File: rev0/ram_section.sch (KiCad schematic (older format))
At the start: 5 parts

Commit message: rev0: finish capture and start routing (woo!)
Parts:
- C44, C45, C46: renamed from C?; footprint (none) -> Capacitor_SMD:C_0402_1005Metric
- IC1: renamed from IC?; footprint BGA256C80P16X16_1400X1400X170 -> luna:lattice_cabga256
- gave numbers to parts that had none: 1
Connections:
- no-connect marks 5 -> 24
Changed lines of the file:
@@
 	1850 1800 1900 1800
 $Comp
-L power:+1V8 #PWR?
+L power:+1V8 #PWR081
 U 1 1 5DE84804
 P 1850 1700
-F 0 "#PWR?" H 1850 1550 50  0001 C CNN
+F 0 "#PWR081" H 1850 1550 50  0001 C CNN
 F 1 "+1V8" H 1864 1873 50  0000 C CNN
 F 2 "" H 1850 1700 50  0001 C CNN
@@
 $EndComp
 $Comp
-L fpgas_and_processors:ECP5-BGA256 IC?
+L fpgas_and_processors:ECP5-BGA256 IC1
 U 3 1 5DE93650
 P 1650 2100
-F 0 "IC?" H 1620 308 50  0000 R CNN
+F 0 "IC1" H 1620 308 50  0000 R CNN
 F 1 "ECP5-BGA256" H 1620 218 50  0000 R CNN
-F 2 "BGA256C80P16X16_1400X1400X170" H -1550 5550 50  0001 L CNN
+F 2 "luna:lattice_cabga256" H -1550 5550 50  0001 L CNN
 F 3 "" H -2000 6500 50  0001 L CNN
 F 4 "FPGA - Field Programmable Gate Array ECP5; 12k LUTs; 1.1V" H -2000 6400 50  0001 L CNN "Description"
@@
 $EndComp
 $Comp
-L support_hardware:S27KS0641 U?
+L support_hardware:S27KS0641 U10
 U 1 1 5DEA1FC4
 P 5400 4850
-F 0 "U?" H 5400 5772 50  0000 C CNN
+F 0 "U10" H 5400 5772 50  0000 C CNN
 F 1 "S27KS0641" H 5400 5682 50  0000 C CNN
 F 2 "pkl_housings_bga:BGA-24_5x5_6.0x8.0mm" H 6000 3950 50  0001 C CNN
@@
 	6550 4250 6550 4000
 $Comp
-L power:+1V8 #PWR?
+L power:+1V8 #PWR084
 U 1 1 5DEA6771
 P 6550 4000
-F 0 "#PWR?" H 6550 3850 50  0001 C CNN
+F 0 "#PWR084" H 6550 3850 50  0001 C CNN
 F 1 "+1V8" H 6564 4173 50  0000 C CNN
 F 2 "" H 6550 4000 50  0001 C CNN
@@
 	6550 5450 6550 5600
 $Comp
-L power:GND #PWR?
+L power:GND #PWR085
 U 1 1 5DEA82D8
 P 6550 5600
-F 0 "#PWR?" H 6550 5350 50  0001 C CNN
+F 0 "#PWR085" H 6550 5350 50  0001 C CNN
 F 1 "GND" H 6554 5428 50  0000 C CNN
 F 2 "" H 6550 5600 50  0001 C CNN
@@
 	6350 4550 6000 4550
 $Comp
-L Device:C C?
+L Device:C C44
 U 1 1 5DEC975A
 P 5100 3050
-F 0 "C?" H 5150 3150 50  0000 L CNN
+F 0 "C44" H 5150 3150 50  0000 L CNN
 F 1 "0.1uF" H 5150 2950 50  0000 L CNN
-F 2 "" H 5138 2900 50  0001 C CNN
+F 2 "Capacitor_SMD:C_0402_1005Metric" H 5138 2900 50  0001 C CNN
 F 3 "~" H 5100 3050 50  0001 C CNN
 	1    5100 3050
@@
 $EndComp
 $Comp
-L Device:C C?
+L Device:C C45
 U 1 1 5DECBE47
 P 5400 3050
-F 0 "C?" H 5450 3150 50  0000 L CNN
+F 0 "C45" H 5450 3150 50  0000 L CNN
 F 1 "0.1uF" H 5450 2950 50  0000 L CNN
-F 2 "" H 5438 2900 50  0001 C CNN
+F 2 "Capacitor_SMD:C_0402_1005Metric" H 5438 2900 50  0001 C CNN
 F 3 "~" H 5400 3050 50  0001 C CNN
 	1    5400 3050
@@
 $EndComp
 $Comp
-L Device:C C?
+L Device:C C46
 U 1 1 5DECC0D1
 P 5700 3050
-F 0 "C?" H 5750 3150 50  0000 L CNN
+F 0 "C46" H 5750 3150 50  0000 L CNN
 F 1 "0.1uF" H 5750 2950 50  0000 L CNN
-F 2 "" H 5738 2900 50  0001 C CNN
+F 2 "Capacitor_SMD:C_0402_1005Metric" H 5738 2900 50  0001 C CNN
 F 3 "~" H 5700 3050 50  0001 C CNN
 	1    5700 3050
@@
 	5400 2800 5700 2800
 $Comp
-L power:+5V #PWR?
+L power:+5V #PWR082
 U 1 1 5DECF10E
 P 5400 2650
-F 0 "#PWR?" H 5400 2500 50  0001 C CNN
+F 0 "#PWR082" H 5400 2500 50  0001 C CNN
 F 1 "+5V" H 5414 2823 50  0000 C CNN
 F 2 "" H 5400 2650 50  0001 C CNN
@@
 Wire Wire Line
 	5400 3300 5400 3400
-Wire Bus Line
-	3100 5650 3100 6050
-Wire Bus Line
-	7200 4950 7200 6050
-$Comp
-L power:GND #PWR?
+$Comp
+L power:GND #PWR083
 U 1 1 5DED5068
 P 5400 3400
-F 0 "#PWR?" H 5400 3150 50  0001 C CNN
+F 0 "#PWR083" H 5400 3150 50  0001 C CNN
 F 1 "GND" H 5404 3228 50  0000 C CNN
 F 2 "" H 5400 3400 50  0001 C CNN
@@
 Text Label 4000 5150 0    50   ~ 0
 RAM_RWDS
+NoConn ~ 2700 2550
+NoConn ~ 2700 2650
+NoConn ~ 2700 2750
+NoConn ~ 2700 2850
+NoConn ~ 2700 2950
+NoConn ~ 2700 3050
+NoConn ~ 2700 3150
+NoConn ~ 2700 3250
+NoConn ~ 2700 3650
+NoConn ~ 2700 3750
+NoConn ~ 2700 3850
+NoConn ~ 2700 4050
+NoConn ~ 2700 4150
+NoConn ~ 2700 4650
+NoConn ~ 2700 4750
+NoConn ~ 2700 4850
+NoConn ~ 2700 5050
+NoConn ~ 2700 5150
+NoConn ~ 2700 5250
+Wire Bus Line
+	3100 5650 3100 6050
+Wire Bus Line
+	7200 4950 7200 6050
 $EndSCHEMATC

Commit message: rev0: throw the parts down so we can get starting routing
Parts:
- U10: footprint pkl_housings_bga:BGA-24_5x5_6.0x8.0mm -> luna:BGA-24_5x5_6.0x8.0mm
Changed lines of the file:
@@
 F 0 "U10" H 5400 5772 50  0000 C CNN
 F 1 "S27KS0641" H 5400 5682 50  0000 C CNN
-F 2 "pkl_housings_bga:BGA-24_5x5_6.0x8.0mm" H 6000 3950 50  0001 C CNN
+F 2 "luna:BGA-24_5x5_6.0x8.0mm" H 6000 3950 50  0001 C CNN
 F 3 "" H 5400 3950 50  0001 C CNN
 F 4 "ANY" H 5400 4850 50  0001 C CNN "Source"

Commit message: rev0: more routing scaffolding
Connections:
- net RAM_DQ3: now also IC1.B9 (PT38A); no longer IC1.E11 (PT51B)
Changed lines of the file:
@@
 	3500 4650 4800 4650
-Wire Wire Line
-	2700 4250 3400 4250
-Wire Wire Line
-	3400 4250 3400 4750
 Wire Wire Line
 	3400 4750 4800 4750
@@
 NoConn ~ 2700 2750
 NoConn ~ 2700 2850
-NoConn ~ 2700 2950
 NoConn ~ 2700 3050
 NoConn ~ 2700 3150
@@
 NoConn ~ 2700 5150
 NoConn ~ 2700 5250
+Wire Wire Line
+	2700 2950 3400 2950
+Wire Wire Line
+	3400 2950 3400 4750
+NoConn ~ 2700 4250
 Wire Bus Line
 	3100 5650 3100 6050

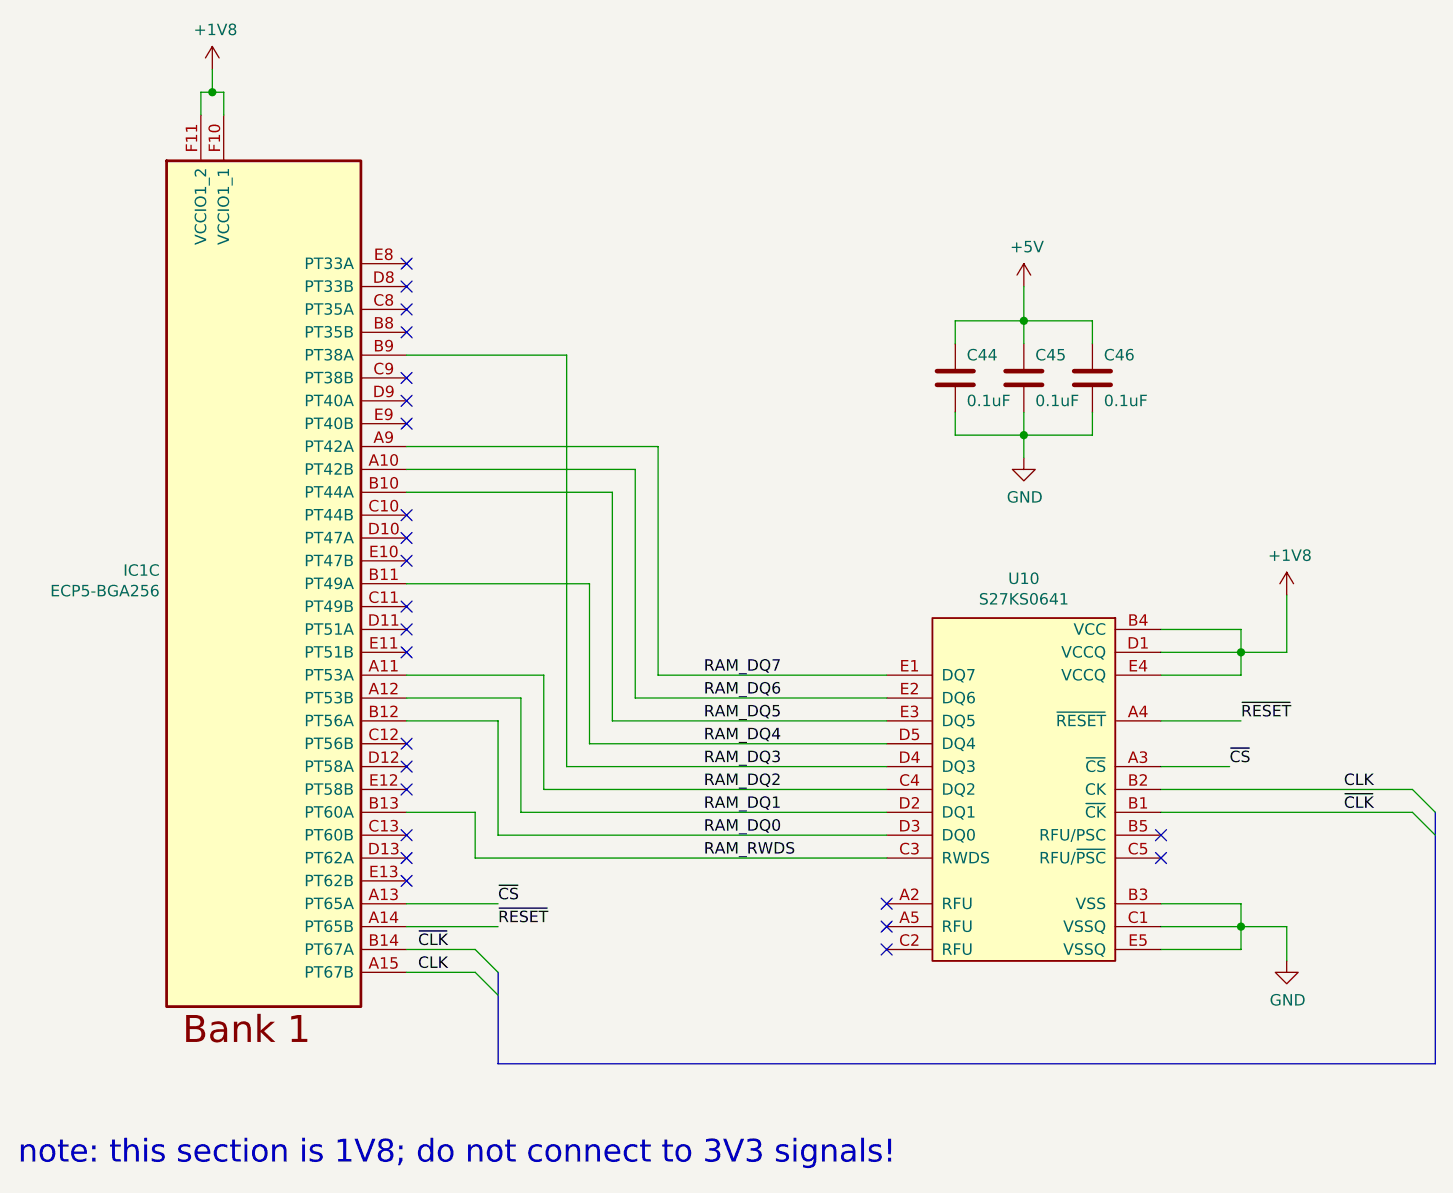
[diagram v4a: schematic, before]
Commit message: rev0: get most of the major routing done
still needs power routing, length matching for the busses,
and routing for the misc control stuff
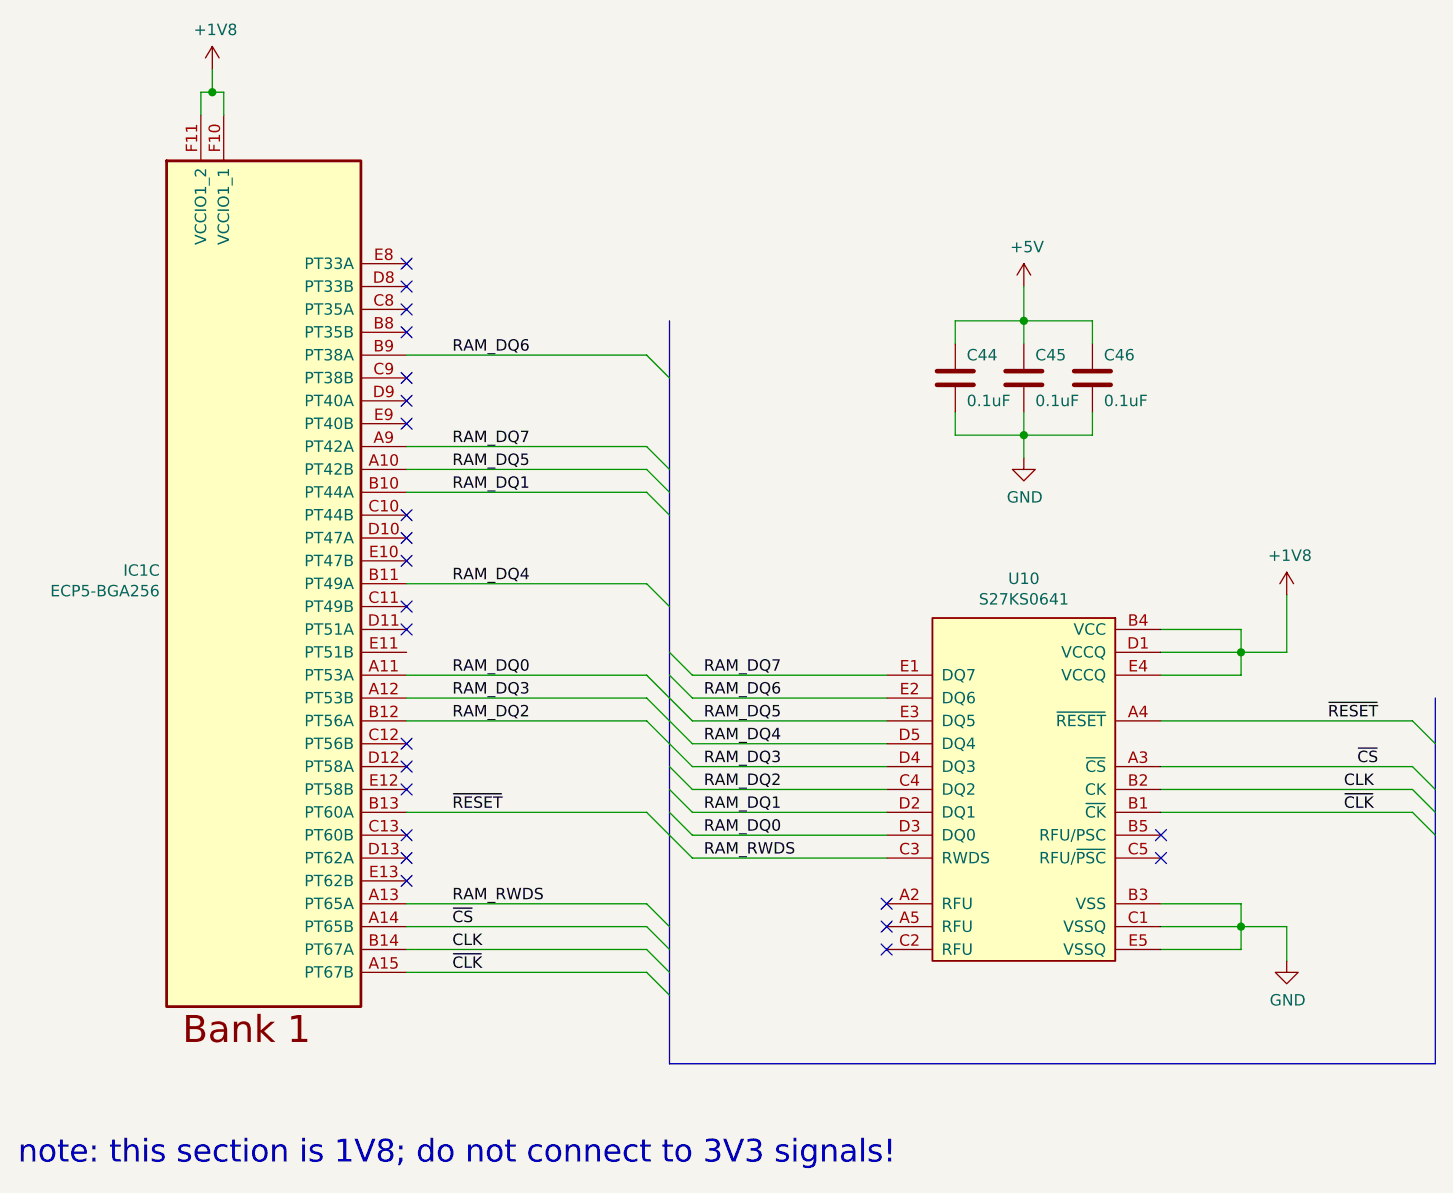
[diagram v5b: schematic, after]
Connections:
- net CLK: now also IC1.B14 (PT67A); no longer IC1.A15 (PT67B)
- net RAM_DQ0: now also IC1.A11 (PT53A); no longer IC1.B12 (PT56A)
- net RAM_DQ1: now also IC1.B10 (PT44A); no longer IC1.A12 (PT53B)
- net RAM_DQ2: now also IC1.B12 (PT56A); no longer IC1.A11 (PT53A)
- net RAM_DQ3: now also IC1.A12 (PT53B); no longer IC1.B9 (PT38A)
- net RAM_DQ5: now also IC1.A10 (PT42B); no longer IC1.B10 (PT44A)
- net RAM_DQ6: now also IC1.B9 (PT38A); no longer IC1.A10 (PT42B)
- net RAM_RWDS: now also IC1.A13 (PT65A); no longer IC1.B13 (PT60A)
- net ~CLK: now also IC1.A15 (PT67B); no longer IC1.B14 (PT67A)
- net ~CS: now also IC1.A14 (PT65B); no longer IC1.A13 (PT65A)
- net ~RESET: now also IC1.B13 (PT60A); no longer IC1.A14 (PT65B)
- no-connect marks 24 -> 23
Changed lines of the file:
@@
 Entry Wire Line
 	7100 4950 7200 5050
-Wire Wire Line
-	2700 5550 3000 5550
-Wire Wire Line
-	2700 5650 3000 5650
-Entry Wire Line
-	3000 5550 3100 5650
-Entry Wire Line
-	3000 5650 3100 5750
 Text Label 6800 4850 0    50   ~ 0
 CLK
 Text Label 6800 4950 0    50   ~ 0
 ~CLK
-Wire Bus Line
-	3100 6050 7200 6050
-Text Label 2750 5550 0    50   ~ 0
+Text Label 2900 5650 0    50   ~ 0
 ~CLK
-Text Label 2750 5650 0    50   ~ 0
+Text Label 2900 5550 0    50   ~ 0
 CLK
-Wire Wire Line
-	2700 3350 3800 3350
-Wire Wire Line
-	3800 3350 3800 4350
-Wire Wire Line
-	3800 4350 4800 4350
-Wire Wire Line
-	2700 3450 3700 3450
-Wire Wire Line
-	3700 3450 3700 4450
-Wire Wire Line
-	3700 4450 4800 4450
-Wire Wire Line
-	2700 3550 3600 3550
-Wire Wire Line
-	3600 3550 3600 4550
-Wire Wire Line
-	3600 4550 4800 4550
-Wire Wire Line
-	2700 3950 3500 3950
-Wire Wire Line
-	3500 3950 3500 4650
-Wire Wire Line
-	3500 4650 4800 4650
-Wire Wire Line
-	3400 4750 4800 4750
-Wire Wire Line
-	2700 4350 3300 4350
-Wire Wire Line
-	3300 4350 3300 4850
-Wire Wire Line
-	3300 4850 4800 4850
-Wire Wire Line
-	2700 4450 3200 4450
-Wire Wire Line
-	3200 4450 3200 4950
-Wire Wire Line
-	3200 4950 4800 4950
-Wire Wire Line
-	2700 4550 3100 4550
-Wire Wire Line
-	3100 4550 3100 5050
-Wire Wire Line
-	3100 5050 4800 5050
-Wire Wire Line
-	4800 5150 3000 5150
-Wire Wire Line
-	3000 5150 3000 4950
-Wire Wire Line
-	3000 4950 2700 4950
 NoConn ~ 4800 5350
 NoConn ~ 4800 5450
@@
 NoConn ~ 6000 5050
 NoConn ~ 6000 5150
-Wire Wire Line
-	2700 5450 3100 5450
-Text Label 3100 5350 0    50   ~ 0
+Text Label 2900 5450 0    50   ~ 0
 ~CS
-Wire Wire Line
-	6000 4750 6300 4750
-Text Label 6300 4750 0    50   ~ 0
+Text Label 6950 4750 2    50   ~ 0
 ~CS
-Wire Wire Line
-	2700 5350 3100 5350
-Text Label 3100 5450 0    50   ~ 0
+Text Label 2900 4950 0    50   ~ 0
 ~RESET
-Text Label 6350 4550 0    50   ~ 0
+Text Label 6950 4550 2    50   ~ 0
 ~RESET
-Wire Wire Line
-	6350 4550 6000 4550
 $Comp
 L Device:C C44
@@
 NoConn ~ 2700 5250
 Wire Wire Line
-	2700 2950 3400 2950
-Wire Wire Line
-	3400 2950 3400 4750
-NoConn ~ 2700 4250
+	4800 4350 3950 4350
+Wire Wire Line
+	3950 4450 4800 4450
+Wire Wire Line
+	4800 4550 3950 4550
+Wire Wire Line
+	4800 4650 3950 4650
+Wire Wire Line
+	4800 4750 3950 4750
+Wire Wire Line
+	4800 4850 3950 4850
+Wire Wire Line
+	4800 4950 3950 4950
+Wire Wire Line
+	4800 5050 3950 5050
+Wire Wire Line
+	4800 5150 3950 5150
+Entry Wire Line
+	3850 4250 3950 4350
+Entry Wire Line
+	3850 4350 3950 4450
+Entry Wire Line
+	3850 4450 3950 4550
+Entry Wire Line
+	3850 4550 3950 4650
+Entry Wire Line
+	3850 4650 3950 4750
+Entry Wire Line
+	3850 4750 3950 4850
+Entry Wire Line
+	3850 4850 3950 4950
+Entry Wire Line
+	3850 4950 3950 5050
+Entry Wire Line
+	3850 5050 3950 5150
 Wire Bus Line
-	3100 5650 3100 6050
+	3850 6050 7200 6050
+Wire Wire Line
+	2700 3350 3750 3350
+Wire Wire Line
+	2700 3450 3750 3450
+Wire Wire Line
+	2700 2950 3750 2950
+Wire Wire Line
+	2700 3550 3750 3550
+Entry Wire Line
+	3750 2950 3850 3050
+Entry Wire Line
+	3750 3350 3850 3450
+Entry Wire Line
+	3750 3450 3850 3550
+Entry Wire Line
+	3750 3550 3850 3650
+Text Label 2900 3350 0    50   ~ 0
+RAM_DQ7
+Text Label 2900 2950 0    50   ~ 0
+RAM_DQ6
+Text Label 2900 3450 0    50   ~ 0
+RAM_DQ5
+Text Label 2900 3550 0    50   ~ 0
+RAM_DQ1
+Wire Wire Line
+	2700 3950 3750 3950
+Entry Wire Line
+	3750 3950 3850 4050
+Text Label 2900 4350 0    50   ~ 0
+RAM_DQ0
+Text Label 2900 3950 0    50   ~ 0
+RAM_DQ4
+Wire Wire Line
+	2700 4450 3750 4450
+Wire Wire Line
+	2700 4350 3750 4350
+Entry Wire Line
+	3750 4350 3850 4450
+Entry Wire Line
+	3750 4450 3850 4550
+Text Label 2900 4450 0    50   ~ 0
+RAM_DQ3
+Wire Wire Line
+	2700 4550 3750 4550
+Entry Wire Line
+	3750 4550 3850 4650
+Text Label 2900 4550 0    50   ~ 0
+RAM_DQ2
+Wire Wire Line
+	2700 4950 3750 4950
+Entry Wire Line
+	3750 4950 3850 5050
+Text Label 2900 5350 0    50   ~ 0
+RAM_RWDS
+Wire Wire Line
+	2700 5350 3750 5350
+Entry Wire Line
+	3750 5350 3850 5450
+Wire Wire Line
+	6000 4550 7100 4550
+Wire Wire Line
+	6000 4750 7100 4750
+Entry Wire Line
+	7100 4750 7200 4850
+Entry Wire Line
+	7100 4550 7200 4650
+Wire Wire Line
+	2700 5450 3750 5450
+Entry Wire Line
+	3750 5450 3850 5550
+Wire Wire Line
+	2700 5550 3750 5550
+Wire Wire Line
+	2700 5650 3750 5650
 Wire Bus Line
-	7200 4950 7200 6050
+	7200 4450 7200 6050
+Wire Bus Line
+	3850 2800 3850 6050
+Entry Wire Line
+	3750 5550 3850 5650
+Entry Wire Line
+	3750 5650 3850 5750
 $EndSCHEMATC

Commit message: hw: address review comments, move to pre-r0.1
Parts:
- removed C44, C45, C46: 0.1uF, Capacitor_SMD:C_0402_1005Metric, symbol Device:C
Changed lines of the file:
@@
 EESchema Schematic File Version 4
 LIBS:luna_rev0-cache
-EELAYER 30 0
+EELAYER 29 0
 EELAYER END
 $Descr A4 11693 8268
@@
 Text Label 6950 4550 2    50   ~ 0
 ~RESET
-$Comp
-L Device:C C44
-U 1 1 5DEC975A
-P 5100 3050
-F 0 "C44" H 5150 3150 50  0000 L CNN
-F 1 "0.1uF" H 5150 2950 50  0000 L CNN
-F 2 "Capacitor_SMD:C_0402_1005Metric" H 5138 2900 50  0001 C CNN
-F 3 "~" H 5100 3050 50  0001 C CNN
-	1    5100 3050
-	1    0    0    -1
-$EndComp
-$Comp
-L Device:C C45
-U 1 1 5DECBE47
-P 5400 3050
-F 0 "C45" H 5450 3150 50  0000 L CNN
-F 1 "0.1uF" H 5450 2950 50  0000 L CNN
-F 2 "Capacitor_SMD:C_0402_1005Metric" H 5438 2900 50  0001 C CNN
-F 3 "~" H 5400 3050 50  0001 C CNN
-	1    5400 3050
-	1    0    0    -1
-$EndComp
-$Comp
-L Device:C C46
-U 1 1 5DECC0D1
-P 5700 3050
-F 0 "C46" H 5750 3150 50  0000 L CNN
-F 1 "0.1uF" H 5750 2950 50  0000 L CNN
-F 2 "Capacitor_SMD:C_0402_1005Metric" H 5738 2900 50  0001 C CNN
-F 3 "~" H 5700 3050 50  0001 C CNN
-	1    5700 3050
-	1    0    0    -1
-$EndComp
-Wire Wire Line
-	5100 2900 5100 2800
-Wire Wire Line
-	5100 2800 5400 2800
-Wire Wire Line
-	5700 2800 5700 2900
-Wire Wire Line
-	5400 2900 5400 2800
-Connection ~ 5400 2800
-Wire Wire Line
-	5400 2800 5700 2800
-$Comp
-L power:+5V #PWR082
-U 1 1 5DECF10E
-P 5400 2650
-F 0 "#PWR082" H 5400 2500 50  0001 C CNN
-F 1 "+5V" H 5414 2823 50  0000 C CNN
-F 2 "" H 5400 2650 50  0001 C CNN
-F 3 "" H 5400 2650 50  0001 C CNN
-	1    5400 2650
-	1    0    0    -1
-$EndComp
-Wire Wire Line
-	5400 2650 5400 2800
-Wire Wire Line
-	5100 3200 5100 3300
-Wire Wire Line
-	5100 3300 5400 3300
-Wire Wire Line
-	5700 3300 5700 3200
-Wire Wire Line
-	5400 3200 5400 3300
-Connection ~ 5400 3300
-Wire Wire Line
-	5400 3300 5700 3300
-Wire Wire Line
-	5400 3300 5400 3400
-$Comp
-L power:GND #PWR083
-U 1 1 5DED5068
-P 5400 3400
-F 0 "#PWR083" H 5400 3150 50  0001 C CNN
-F 1 "GND" H 5404 3228 50  0000 C CNN
-F 2 "" H 5400 3400 50  0001 C CNN
-F 3 "" H 5400 3400 50  0001 C CNN
-	1    5400 3400
-	1    0    0    -1
-$EndComp
 Text Label 4000 4350 0    50   ~ 0
 RAM_DQ7
@@
 Wire Wire Line
 	2700 5650 3750 5650
+Entry Wire Line
+	3750 5550 3850 5650
+Entry Wire Line
+	3750 5650 3850 5750
 Wire Bus Line
 	7200 4450 7200 6050
 Wire Bus Line
 	3850 2800 3850 6050
-Entry Wire Line
-	3750 5550 3850 5650
-Entry Wire Line
-	3750 5650 3850 5750
 $EndSCHEMATC
